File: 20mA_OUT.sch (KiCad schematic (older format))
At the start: 29 parts, among them Q1 BSS123, Q2 BSS123, Q3 BSS123, Q4 BSS123, U5 LM324

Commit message: Finished the schematic, except for maybe a couple test points.
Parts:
- removed U5: LM324, Package_DIP:DIP-14_W7.62mm, symbol Amplifier_Operational:LM324
- added U7: TLV9004xRUCR, Package_SO:SOIC-14_3.9x8.7mm_P1.27mm, symbol Amplifier_Operational:TLV9004xRUCR
- renumbered C19 to C28, C20 to C29, C21 to C30, C22 to C31, C23 to C32, C24 to C33, C25 to C34, C26 to C35, R26 to R29, R27 to R30, R28 to R31, R29 to R32, R30 to R33, R31 to R34, R32 to R35, R33 to R36, R34 to R37, R35 to R38, R36 to R39, R37 to R40, R38 to R41, R39 to R42, R40 to R43, R41 to R44
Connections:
- net labels added: +5V
- net labels removed: +10V

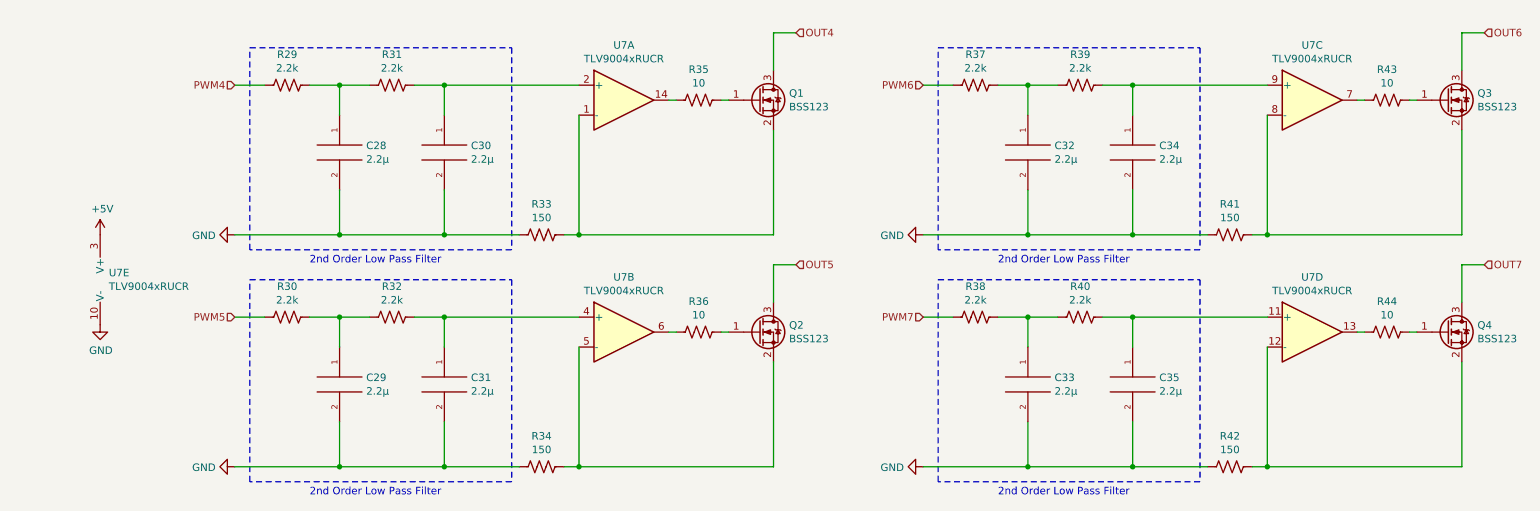
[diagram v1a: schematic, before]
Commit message: Routing for all analog outputs
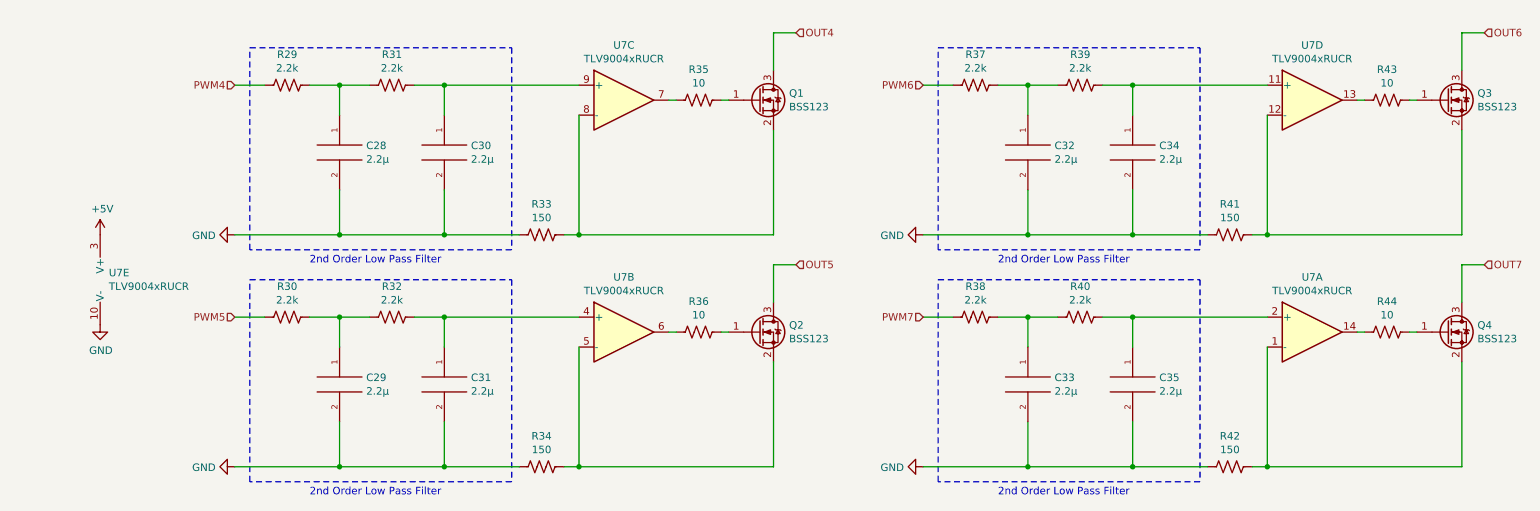
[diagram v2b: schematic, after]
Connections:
- net at C30.1, R31.1: now also U7.9 (+); no longer U7.2 (+)
- net at Q1.2 (S), R33.1: now also U7.8 (-); no longer U7.1 (-)
- net at R35.2: now also U7.7; no longer U7.14
- net at Q3.2 (S), R41.1: now also U7.12 (-); no longer U7.8 (-)
- net at Q4.2 (S), R42.1: now also U7.1 (-); no longer U7.12 (-)
- net at C34.1, R39.1: now also U7.11 (+); no longer U7.9 (+)
- net at R43.2: now also U7.13; no longer U7.7
- net at C35.1, R40.1: now also U7.2 (+); no longer U7.11 (+)
- net at R44.2: now also U7.14; no longer U7.13
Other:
- moved on the sheet: U7C
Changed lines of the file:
@@
-$Comp
-L Amplifier_Operational:TLV9004xRUCR U7
-U 1 1 61E39D41
-P 4450 2800
-F 0 "U7" H 4450 3167 50  0000 C CNN
-F 1 "TLV9004xRUCR" H 4450 3076 50  0000 C CNN
-F 2 "Package_SO:SOIC-14_3.9x8.7mm_P1.27mm" H 4450 2800 50  0001 C CNN
-F 3 "http://www.ti.com/lit/ds/symlink/tlv9004.pdf" H 4500 3000 50  0001 C CNN
-	1    4450 2800
-	1    0    0    -1
-$EndComp
 $Comp
 L Amplifier_Operational:TLV9004xRUCR U7
@@
 L Amplifier_Operational:TLV9004xRUCR U7
 U 3 1 61E43B0E
-P 9050 2800
-F 0 "U7" H 9050 3167 50  0000 C CNN
-F 1 "TLV9004xRUCR" H 9050 3076 50  0000 C CNN
-F 2 "Package_SO:SOIC-14_3.9x8.7mm_P1.27mm" H 9050 2800 50  0001 C CNN
-F 3 "http://www.ti.com/lit/ds/symlink/tlv9004.pdf" H 9100 3000 50  0001 C CNN
-	3    9050 2800
-	1    0    0    -1
-$EndComp
-$Comp
-L Amplifier_Operational:TLV9004xRUCR U7
-U 4 1 61E44681
-P 9050 4350
-F 0 "U7" H 9050 4717 50  0000 C CNN
-F 1 "TLV9004xRUCR" H 9050 4626 50  0000 C CNN
-F 2 "Package_SO:SOIC-14_3.9x8.7mm_P1.27mm" H 9050 4350 50  0001 C CNN
-F 3 "http://www.ti.com/lit/ds/symlink/tlv9004.pdf" H 9100 4550 50  0001 C CNN
-	4    9050 4350
+P 4450 2800
+F 0 "U7" H 4450 3167 50  0000 C CNN
+F 1 "TLV9004xRUCR" H 4450 3076 50  0000 C CNN
+F 2 "Package_SO:SOIC-14_3.9x8.7mm_P1.27mm" H 4450 2800 50  0001 C CNN
+F 3 "http://www.ti.com/lit/ds/symlink/tlv9004.pdf" H 4500 3000 50  0001 C CNN
+	3    4450 2800
 	1    0    0    -1
 $EndComp
@@
 	1    0    0    -1
 $EndComp
+$Comp
+L Amplifier_Operational:TLV9004xRUCR U7
+U 1 1 61249F21
+P 9050 4350
+F 0 "U7" H 9050 4717 50  0000 C CNN
+F 1 "TLV9004xRUCR" H 9050 4626 50  0000 C CNN
+F 2 "Package_SO:SOIC-14_3.9x8.7mm_P1.27mm" H 9050 4350 50  0001 C CNN
+F 3 "http://www.ti.com/lit/ds/symlink/tlv9004.pdf" H 9100 4550 50  0001 C CNN
+	1    9050 4350
+	1    0    0    -1
+$EndComp
+$Comp
+L Amplifier_Operational:TLV9004xRUCR U7
+U 4 1 612554CE
+P 9050 2800
+F 0 "U7" H 9050 3167 50  0000 C CNN
+F 1 "TLV9004xRUCR" H 9050 3076 50  0000 C CNN
+F 2 "Package_SO:SOIC-14_3.9x8.7mm_P1.27mm" H 9050 2800 50  0001 C CNN
+F 3 "http://www.ti.com/lit/ds/symlink/tlv9004.pdf" H 9100 3000 50  0001 C CNN
+	4    9050 2800
+	1    0    0    -1
+$EndComp
